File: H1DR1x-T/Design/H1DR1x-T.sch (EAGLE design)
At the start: 30 parts, among them P1 HEXABIT_17.32_NO_P6, P2 RS-485, U1 STM32G0B1CEU6QFN_B1CEU6_STM-L, U2 MAX14840EASAT, X1 XTALL_CSTCE8M00G52

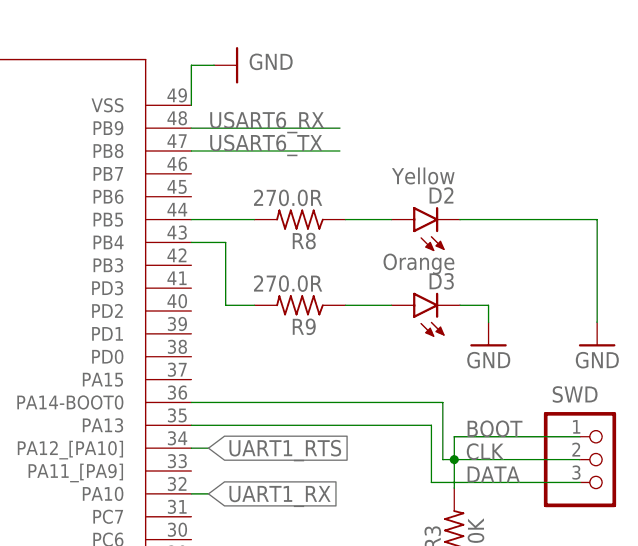
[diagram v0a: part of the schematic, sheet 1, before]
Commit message: - Fixed issues in PCB. - Regenerated output files.
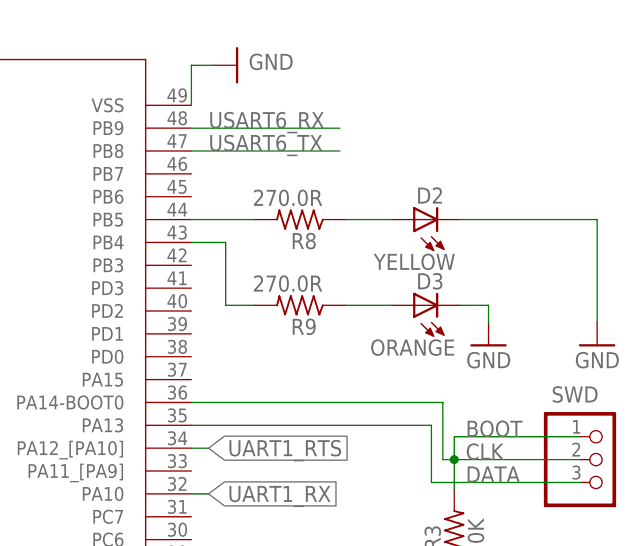
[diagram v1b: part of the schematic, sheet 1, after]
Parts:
- D2: value Yellow -> YELLOW; device HEXABITZ_USER_INTERFACE_PARTS:LEDCHIP-LED0805 -> HEXABITZ_USER_INTERFACE_PARTS:VLMS1300-GS08; OCTOPART_URL (none) -> https://octopart.com/vlms1300-gs08-vishay-21709201?r=sp&s=_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
- D3: value Orange -> ORANGE; device HEXABITZ_USER_INTERFACE_PARTS:LEDCHIP-LED0805 -> HEXABITZ_USER_INTERFACE_PARTS:VLMS1300-GS08; OCTOPART_URL (none) -> https://octopart.com/vlms1300-gs08-vishay-21709201?r=sp&s=_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
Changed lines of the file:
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@@
 <part name="R8" library="HEXABITZ_RCLS" library_urn="urn:adsk.eagle:library:20064561" deviceset="R-0603" device="" package3d_urn="urn:adsk.eagle:package:1435818/6" value="270.0R"/>
 <part name="R9" library="HEXABITZ_RCLS" library_urn="urn:adsk.eagle:library:20064561" deviceset="R-0603" device="" package3d_urn="urn:adsk.eagle:package:1435818/6" value="270.0R"/>
-<part name="D2" library="HEXABITZ_USER_INTERFACE_PARTS" library_urn="urn:adsk.eagle:library:20064563" deviceset="LED" device="CHIP-LED0805" package3d_urn="urn:adsk.eagle:package:15818/2" value="Yellow"/>
-<part name="D3" library="HEXABITZ_USER_INTERFACE_PARTS" library_urn="urn:adsk.eagle:library:20064563" deviceset="LED" device="CHIP-LED0805" package3d_urn="urn:adsk.eagle:package:15818/2" value="Orange"/>
 <part name="GND4" library="supply1" library_urn="urn:adsk.eagle:library:371" deviceset="GND" device=""/>
 <part name="GND7" library="supply1" library_urn="urn:adsk.eagle:library:371" deviceset="GND" device=""/>
+<part name="D2" library="HEXABITZ_USER_INTERFACE_PARTS" library_urn="urn:adsk.eagle:library:20064563" deviceset="VLMS1300-GS08" device="" package3d_urn="urn:adsk.eagle:package:20064571/3" value="YELLOW">
+<attribute name="OCTOPART_URL" value="https://octopart.com/vlms1300-gs08-vishay-21709201?r=sp&amp;s=_gcP4_q8T1SC6PJQPTQ9yA"/>
+</part>
+<part name="D3" library="HEXABITZ_USER_INTERFACE_PARTS" library_urn="urn:adsk.eagle:library:20064563" deviceset="VLMS1300-GS08" device="" package3d_urn="urn:adsk.eagle:package:20064571/3" value="ORANGE">
+<attribute name="OCTOPART_URL" value="https://octopart.com/vlms1300-gs08-vishay-21709201?r=sp&amp;s=_gcP4_q8T1SC6PJQPTQ9yA"/>
+</part>
 </parts>
 <sheets>
@@
 <attribute name="VALUE" x="226.06" y="169.037" size="1.778" layer="96" rot="R180"/>
 </instance>
-<instance part="D2" gate="G$1" x="236.22" y="175.26" smashed="yes" rot="R90">
-<attribute name="NAME" x="240.792" y="178.816" size="1.778" layer="95" rot="R180"/>
-<attribute name="VALUE" x="240.792" y="180.975" size="1.778" layer="96" rot="R180"/>
-</instance>
-<instance part="D3" gate="G$1" x="236.22" y="165.735" smashed="yes" rot="R90">
-<attribute name="NAME" x="240.792" y="169.291" size="1.778" layer="95" rot="R180"/>
-<attribute name="VALUE" x="240.792" y="171.45" size="1.778" layer="96" rot="R180"/>
-</instance>
 <instance part="GND4" gate="1" x="244.475" y="161.29" smashed="yes" rot="MR0">
 <attribute name="VALUE" x="247.015" y="158.75" size="1.778" layer="96" rot="MR0"/>
@@
 <instance part="GND7" gate="1" x="256.54" y="161.29" smashed="yes" rot="MR0">
 <attribute name="VALUE" x="259.08" y="158.75" size="1.778" layer="96" rot="MR0"/>
+</instance>
+<instance part="D2" gate="G$1" x="236.22" y="175.26" smashed="yes" rot="R180">
+<attribute name="NAME" x="239.522" y="178.816" size="1.778" layer="95" rot="R180"/>
+<attribute name="VALUE" x="240.792" y="171.45" size="1.778" layer="96" rot="R180"/>
+</instance>
+<instance part="D3" gate="G$1" x="236.22" y="165.735" smashed="yes" rot="R180">
+<attribute name="NAME" x="239.522" y="169.291" size="1.778" layer="95" rot="R180"/>
+<attribute name="VALUE" x="240.792" y="161.925" size="1.778" layer="96" rot="R180"/>
 </instance>
 </instances>
@@
 <segment>
 <pinref part="GND4" gate="1" pin="GND"/>
-<pinref part="D3" gate="G$1" pin="C"/>
 <wire x1="244.475" y1="163.83" x2="244.475" y2="165.735" width="0.1524" layer="91"/>
 <wire x1="244.475" y1="165.735" x2="241.3" y2="165.735" width="0.1524" layer="91"/>
-</segment>
-<segment>
-<pinref part="D2" gate="G$1" pin="C"/>
+<pinref part="D3" gate="G$1" pin="C"/>
+</segment>
+<segment>
 <pinref part="GND7" gate="1" pin="GND"/>
 <wire x1="241.3" y1="175.26" x2="256.54" y2="175.26" width="0.1524" layer="91"/>
 <wire x1="256.54" y1="175.26" x2="256.54" y2="163.83" width="0.1524" layer="91"/>
+<pinref part="D2" gate="G$1" pin="C"/>
 </segment>
 </net>
@@
 <segment>
 <pinref part="R9" gate="G$1" pin="1"/>
+<wire x1="228.6" y1="165.735" x2="233.68" y2="165.735" width="0.1524" layer="91"/>
 <pinref part="D3" gate="G$1" pin="A"/>
-<wire x1="228.6" y1="165.735" x2="233.68" y2="165.735" width="0.1524" layer="91"/>
 </segment>
 </net>
@@
 <segment>
 <pinref part="R8" gate="G$1" pin="1"/>
+<wire x1="228.6" y1="175.26" x2="233.68" y2="175.26" width="0.1524" layer="91"/>
 <pinref part="D2" gate="G$1" pin="A"/>
-<wire x1="228.6" y1="175.26" x2="233.68" y2="175.26" width="0.1524" layer="91"/>
-</segment>
-</net>
+</segment>
+</net>

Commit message: Everything is finished. I fixed some issues and reviewed everything.
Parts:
- removed C1: 1uF, HEXABITZ_RCLS:C-0805
- added C2: 1uF, HEXABITZ_RCLS:C-0805
- C10, C12: device Hexabitz:C-0603 -> HEXABITZ_RCLS:C-0603
- C11: device Hexabitz:C-0805-POL -> HEXABITZ_RCLS:C-0805-POL
- P2: device Hexabitz:1546111-2 -> HEXABITZ_CONNECTION_PARTS:1546111-2
- R1: value 0.0R -> 270R; MFN Yageo -> (none); MPN RC0603JR-070RL -> (none); OCTOPART_URL https://octopart.com/rc0603jr-070rl-yageo-1241539?r=sp&s=X2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 -> (none); RESISTANCE 0.0 Ohm -> (none)
- R2: value 270R -> 0.0R; MFN (none) -> Yageo; MPN (none) -> RC0603JR-070RL; OCTOPART_URL (none) -> https://octopart.com/rc0603jr-070rl-yageo-1241539?r=sp&s=X2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; RESISTANCE (none) -> 0.0 Ohm
- R4, R6, R7: device Hexabitz:R-0603 -> HEXABITZ_RCLS:R-0603
- R5: device Hexabitz:R-0805 -> HEXABITZ_RCLS:R-0603
- R8, R9: value 270.0R -> 270R
- U2: value MAX14840EASAT -> MAX14840EASA+T; device Hexabitz:MAX14840EASAT -> HEXABITZ_ICs:MAX14840EASA+T
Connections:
- net N$7 renamed TB
- net N$8 renamed TA
- removed net N$11: R9.2, U1.PB4
- removed net N$9: R8.2, U1.PB5
- removed net UART1_RTS: R6.1, U1.PA12_[PA10], U2.!RE, U2.DE
- removed net UART1_RX: U1.PA10, U2.RO
- removed net UART1_TX: U1.PA9, U2.DI
- new net RX_LED: R9.2, U1.PB13
- new net TX_LED: R8.2, U1.PB14
- new net USART1_RX: P1.SD4, U1.PA10
- new net USART1_TX: P1.SU4, U1.PA9
- new net USART3_RTS: R6.1, U1.PA15, U2.!RE, U2.DE
- net GND: now also R2.1; no longer R1.1
- net N$1: now also R1.2; no longer R2.2
- net N$3: now also R1.1; no longer R2.1
- net USART3_RX: now also U1.PB9, U2.RO; no longer P1.SD5, U1.PB11
- net USART3_TX: now also U1.PB8, U2.DI; no longer P1.SU5, U1.PB10
- net USART4_RX: now also P1.SD1; no longer P1.SD3
- net USART4_TX: now also P1.SU1; no longer P1.SU3
- net USART5_RX: now also P1.SD5, U1.PD2; no longer P1.SD4, U1.PB1
- net USART5_TX: now also P1.SU5, U1.PD3; no longer P1.SU4, U1.PB0
- net USART6_RX: now also P1.SD3, U1.PA5; no longer P1.SD1, U1.PB9
- net USART6_TX: now also P1.SU3, U1.PA4; no longer P1.SU1, U1.PB8
- net VDDA: now also C2.1; no longer C1.1
- net VSSA: now also C2.2, R2.2; no longer C1.2, R1.2
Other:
- moved on the sheet: C10, C11, C12, C3, C4, C5, C6, D1, D2, D3, D5, FB1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
